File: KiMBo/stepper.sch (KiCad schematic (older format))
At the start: 13 parts, among them U16 74x2G00, U17 74LS20, U18 74HC595, U19 74HC595, U20 74HC595

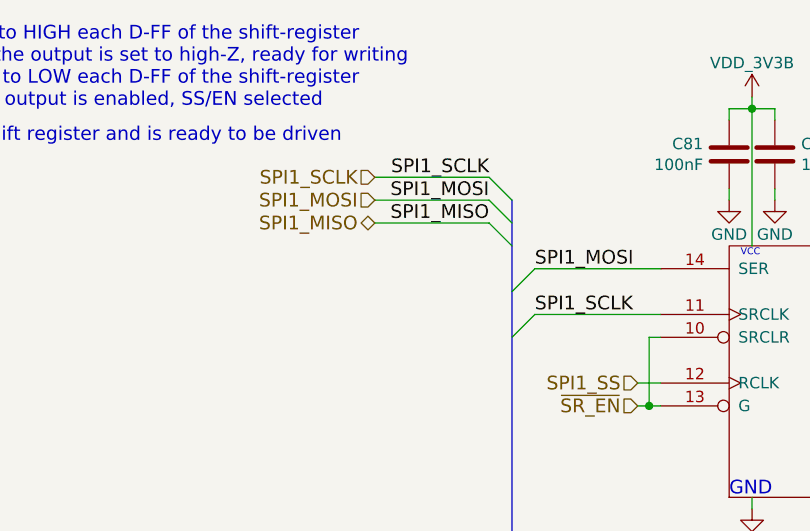
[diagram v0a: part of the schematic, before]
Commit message: Change the endstop RC filter
Lower the time constant

Reduce the series resistor to 100Ohms
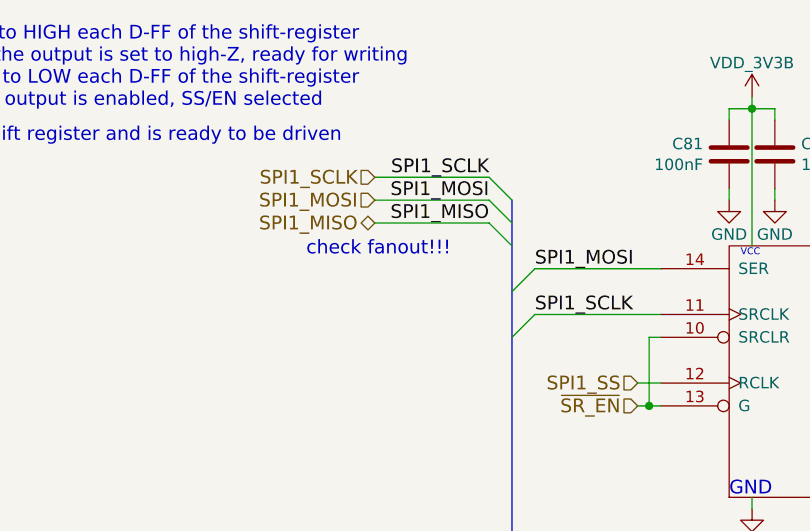
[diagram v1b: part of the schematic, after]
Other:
- note added: "check fanout!!!"
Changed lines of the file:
@@
 Wire Wire Line
 	3000 6800 2900 6800
+Text Notes 3400 1600 0    60   ~ 0
+check fanout!!!
 $EndSCHEMATC

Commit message: Connect X and Z stepper driver open-drain DIAG0 and DIAG1 lines together
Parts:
- removed C79, C80: 100nF, Capacitors_SMD:C_0402, symbol C
- removed U16: 74x2G00, symbol 74x2G00
- removed U17: 74LS20, symbol 74LS20
- renumbered C81 to C79, C82 to C80, C83 to C81, C84 to C82, C85 to C83, C86 to C84, U18 to U16, U19 to U17, U20 to U18
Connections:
- net labels removed: X0_FAULT, X0_SG, X1_FAULT, X1_SG, Z0_FAULT, Z0_SG, Z1_FAULT, Z1_SG, Z2_FAULT, Z2_SG
- wire segments 209 -> 177

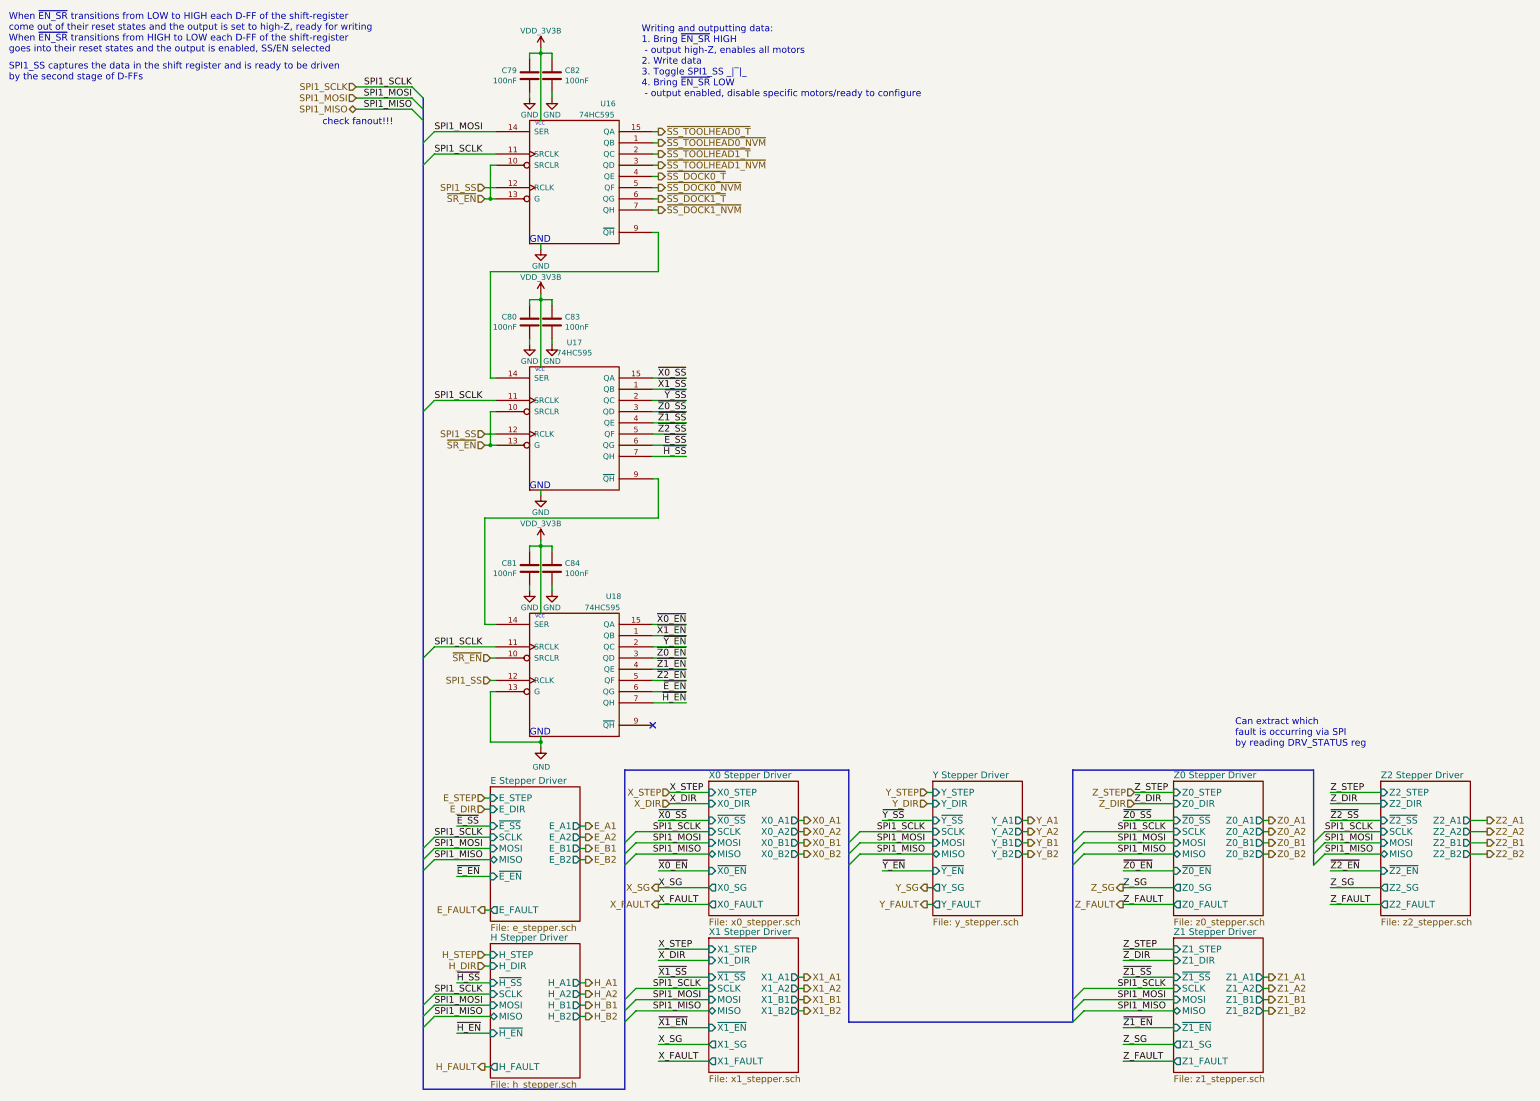
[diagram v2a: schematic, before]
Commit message: Leave SPI0 free for a display, reassign pins so SPI1 is available
Fix some typos/errors
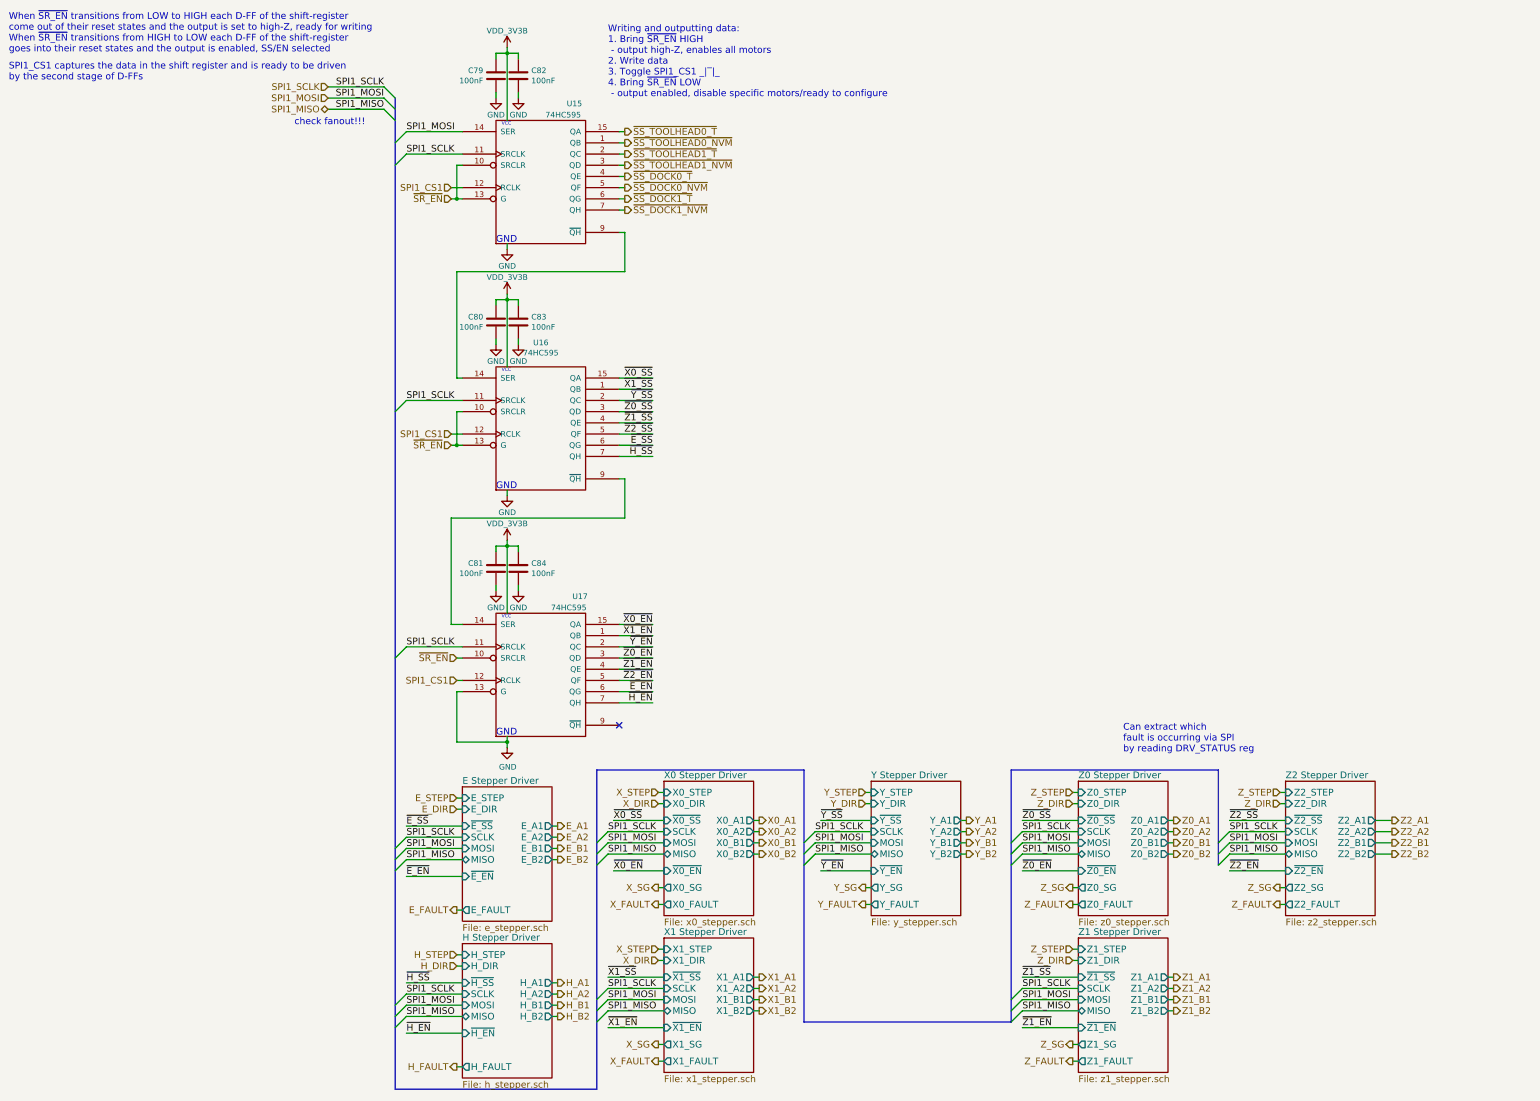
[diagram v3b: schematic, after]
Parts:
- renumbered U16 to U15, U17 to U16, U18 to U17
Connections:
- net SPI1_SS renamed SPI1_CS1
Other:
- note added: "SPI1_CS1 captures the data in the shift register and is ready to be driven\nby the second stage of D-FFs"
- note added: "When ~SR_EN~ transitions from LOW to HIGH each D-FF of the shift-register\ncome out of their reset states and the output is set to high-Z, ready for writing\nWhen ~SR_EN~ transitions from HIGH to LOW each D-FF of the shift-register\ngoes into their reset states and the output is enabled, SS/EN selected"
- note added: "Writing and outputting data:\n1. Bring ~SR_EN~ HIGH\n - output high-Z, enables all motors\n2. Write data\n3. Toggle SPI1_CS1 _|‾|_\n4. Bring ~SR_EN~ LOW\n - output enabled, disable specific motors/ready to configure"
- note removed: "SPI1_SS captures the data in the shift register and is ready to be driven\nby the second stage of D-FFs"
- note removed: "When ~EN_SR~ transitions from LOW to HIGH each D-FF of the shift-register\ncome out of their reset states and the output is set to high-Z, ready for writing\nWhen ~EN_SR~ transitions from HIGH to LOW each D-FF of the shift-register\ngoes into their reset states and the output is enabled, SS/EN selected"
- note removed: "Writing and outputting data:\n1. Bring ~EN_SR~ HIGH\n - output high-Z, enables all motors\n2. Write data\n3. Toggle SPI1_SS _|‾|_\n4. Bring ~EN_SR~ LOW\n - output enabled, disable specific motors/ready to configure"
- moved on the sheet: C79, C80, C81, C82, C83, C84, U15, U16, U17

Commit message: Use fixed 5V LM2592HV Buck, include SPI0 header for LCD
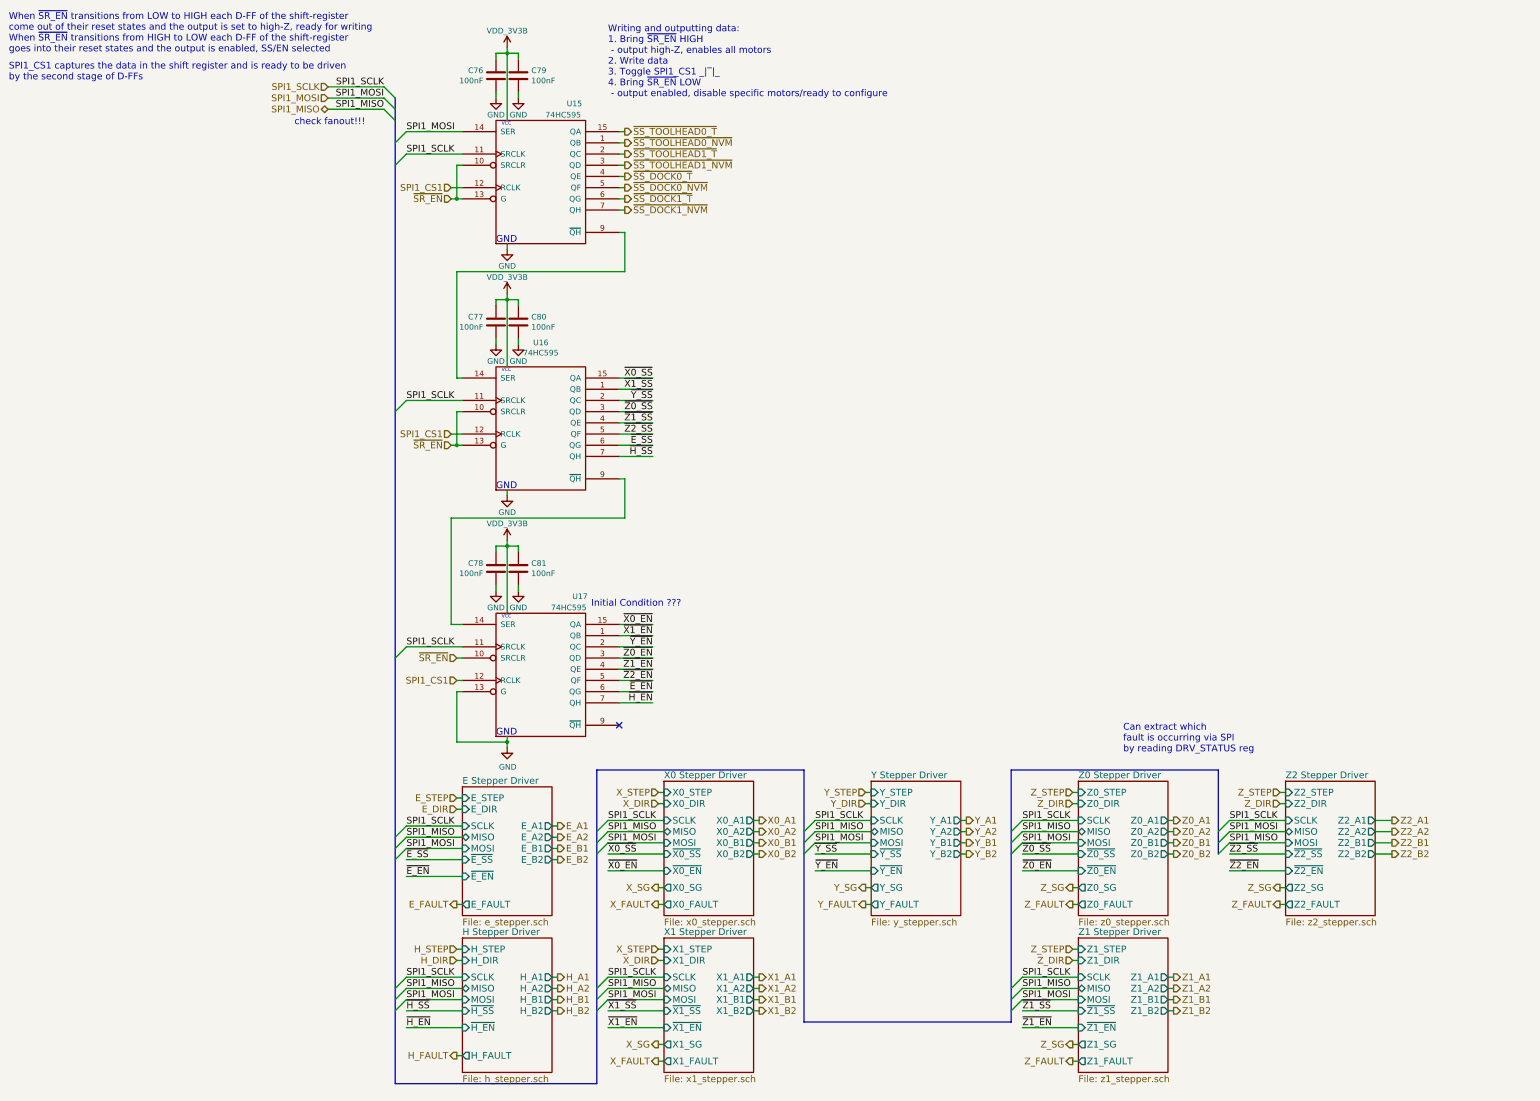
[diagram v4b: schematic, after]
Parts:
- renumbered C79 to C76, C80 to C77, C81 to C78, C82 to C79, C83 to C80, C84 to C81
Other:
- note added: "Initial Condition ???"

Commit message: Assocate more footprints
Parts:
- C76, C77, C78, C79, C80, C81: footprint Capacitors_SMD:C_0402 -> Capacitors_SMD:C_0603
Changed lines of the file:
@@
 F 0 "C76" H 5064 1196 50  0000 L CNN
 F 1 "100nF" H 5064 1105 50  0000 L CNN
-F 2 "Capacitors_SMD:C_0402" H 4988 1000 50  0001 C CNN
+F 2 "Capacitors_SMD:C_0603" H 4988 1000 50  0001 C CNN
 F 3 "" H 4950 1150 50  0000 C CNN
 	1    4950 1150
@@
 F 0 "C79" H 5035 1104 50  0000 R CNN
 F 1 "100nF" H 5035 1195 50  0000 R CNN
-F 2 "Capacitors_SMD:C_0402" H 5188 1000 50  0001 C CNN
+F 2 "Capacitors_SMD:C_0603" H 5188 1000 50  0001 C CNN
 F 3 "" H 5150 1150 50  0000 C CNN
 	1    5150 1150
@@
 F 0 "C78" H 5064 5596 50  0000 L CNN
 F 1 "100nF" H 5064 5505 50  0000 L CNN
-F 2 "Capacitors_SMD:C_0402" H 4988 5400 50  0001 C CNN
+F 2 "Capacitors_SMD:C_0603" H 4988 5400 50  0001 C CNN
 F 3 "" H 4950 5550 50  0000 C CNN
 	1    4950 5550
@@
 F 0 "C81" H 5265 5596 50  0000 L CNN
 F 1 "100nF" H 5265 5505 50  0000 L CNN
-F 2 "Capacitors_SMD:C_0402" H 5188 5400 50  0001 C CNN
+F 2 "Capacitors_SMD:C_0603" H 5188 5400 50  0001 C CNN
 F 3 "" H 5150 5550 50  0000 C CNN
 	1    5150 5550
@@
 F 0 "C77" H 5064 3396 50  0000 L CNN
 F 1 "100nF" H 5064 3305 50  0000 L CNN
-F 2 "Capacitors_SMD:C_0402" H 4988 3200 50  0001 C CNN
+F 2 "Capacitors_SMD:C_0603" H 4988 3200 50  0001 C CNN
 F 3 "" H 4950 3350 50  0000 C CNN
 	1    4950 3350
@@
 F 0 "C80" H 5265 3396 50  0000 L CNN
 F 1 "100nF" H 5265 3305 50  0000 L CNN
-F 2 "Capacitors_SMD:C_0402" H 5188 3200 50  0001 C CNN
+F 2 "Capacitors_SMD:C_0603" H 5188 3200 50  0001 C CNN
 F 3 "" H 5150 3350 50  0000 C CNN
 	1    5150 3350
@@
 	8300 8550 8250 8550
 Wire Bus Line
-	5850 10150 4050 10150
-Wire Bus Line
-	5850 7350 5850 10150
+	4050 10150 5850 10150
+Wire Bus Line
+	5850 10150 5850 7350
 Wire Bus Line
 	5850 7350 7700 7350
@@
 	7700 7350 7700 9600
 Wire Bus Line
-	9550 9600 7700 9600
-Wire Bus Line
-	9550 7350 9550 9600
+	7700 9600 9550 9600
+Wire Bus Line
+	9550 9600 9550 7350
 Wire Bus Line
 	9550 7350 11400 7350

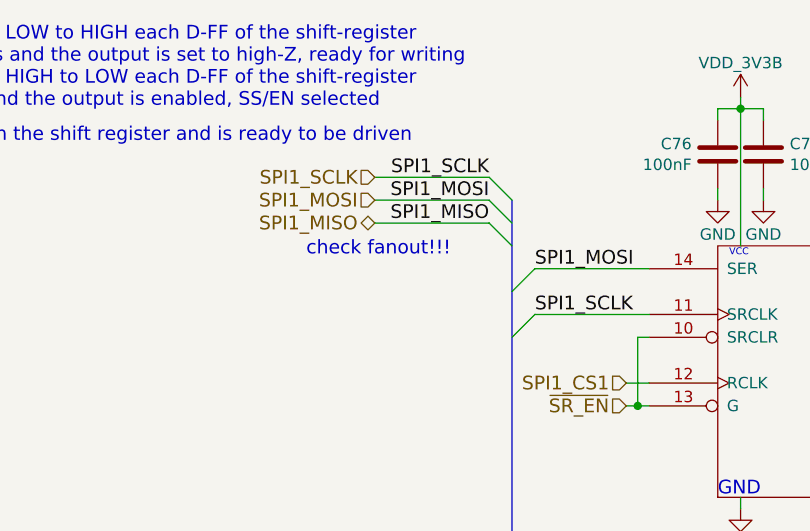
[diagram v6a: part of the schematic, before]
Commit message: Create more footprints and add more associations
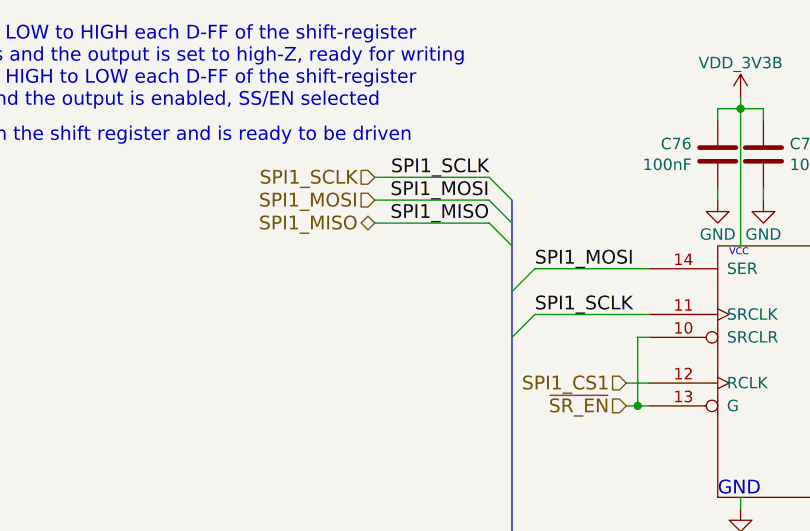
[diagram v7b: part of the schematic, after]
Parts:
- U15, U16, U17: footprint (none) -> Housings_SSOP:TSSOP-16_4.4x5mm_Pitch0.65mm
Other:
- note removed: "check fanout!!!"
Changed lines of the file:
@@
 F 0 "U15" H 5650 2800 50  0000 C CNN
 F 1 "74HC595" H 5550 2700 50  0000 C CNN
-F 2 "" H 5350 2100 50  0001 C CNN
+F 2 "Housings_SSOP:TSSOP-16_4.4x5mm_Pitch0.65mm" H 5350 2100 50  0001 C CNN
 F 3 "" H 5350 2100 50  0000 C CNN
 	1    5350 2100
@@
 F 0 "U16" H 5350 5066 50  0000 C CNN
 F 1 "74HC595" H 5350 4975 50  0000 C CNN
-F 2 "" H 5350 4300 50  0001 C CNN
+F 2 "Housings_SSOP:TSSOP-16_4.4x5mm_Pitch0.65mm" H 5350 4300 50  0001 C CNN
 F 3 "" H 5350 4300 50  0000 C CNN
 	1    5350 4300
@@
 F 0 "U17" H 5700 7200 50  0000 C CNN
 F 1 "74HC595" H 5600 7100 50  0000 C CNN
-F 2 "" H 5350 6500 50  0001 C CNN
+F 2 "Housings_SSOP:TSSOP-16_4.4x5mm_Pitch0.65mm" H 5350 6500 50  0001 C CNN
 F 3 "" H 5350 6500 50  0000 C CNN
 	1    5350 6500
@@
 Text HLabel 3450 1350 0    60   Input ~ 0
 SPI1_MOSI
-Text Notes 3150 1600 0    60   ~ 0
-check fanout!!!
 Wire Wire Line
 	5050 900  5050 1550

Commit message: Add more footprints and more associations, one association left!
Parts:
- added R131, R132, R133, R134, R135, R136, R137, R138, R139: 4.7kΩ, Resistors_SMD:R_0603, symbol R
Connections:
- net VCC: now also R131.1, R132.1, R133.1, R134.1, R135.1, R136.1, R137.1, R138.1, R139.1
- net ~SR_EN: now also R131.2
- net ~SS_DOCK0_NVM: now also R137.2
- net ~SS_DOCK0_T: now also R136.2
- net ~SS_DOCK1_NVM: now also R139.2
- net ~SS_DOCK1_T: now also R138.2
- net ~SS_TOOLHEAD0_NVM: now also R133.2
- net ~SS_TOOLHEAD0_T: now also R132.2
- net ~SS_TOOLHEAD1_NVM: now also R135.2
- net ~SS_TOOLHEAD1_T: now also R134.2
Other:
- note added: "Writing and outputting data:\n1. Bring ~SR_EN~ HIGH\n - output high-Z (pull-ups)\n2. Write data\n3. Toggle SPI1_CS1 _|‾|_\n4. Bring ~SR_EN~ LOW\n - output enabled, disable specific motors/ready to configure"
- note removed: "Writing and outputting data:\n1. Bring ~SR_EN~ HIGH\n - output high-Z, enables all motors\n2. Write data\n3. Toggle SPI1_CS1 _|‾|_\n4. Bring ~SR_EN~ LOW\n - output enabled, disable specific motors/ready to configure"
